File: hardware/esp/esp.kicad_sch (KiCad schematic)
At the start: 37 parts, among them J1 USB_C_Receptacle_USB2.0_16P, J2 Conn_01x02, J3 USB_C_Receptacle_USB2.0_16P, J4 Conn_01x01_Pin, SW1 RESET, SW2 BOOT, U1 AMS1117-3.3, U2 ESP32-S3-WROOM-1, U6 CP2102N-Axx-xQFN20

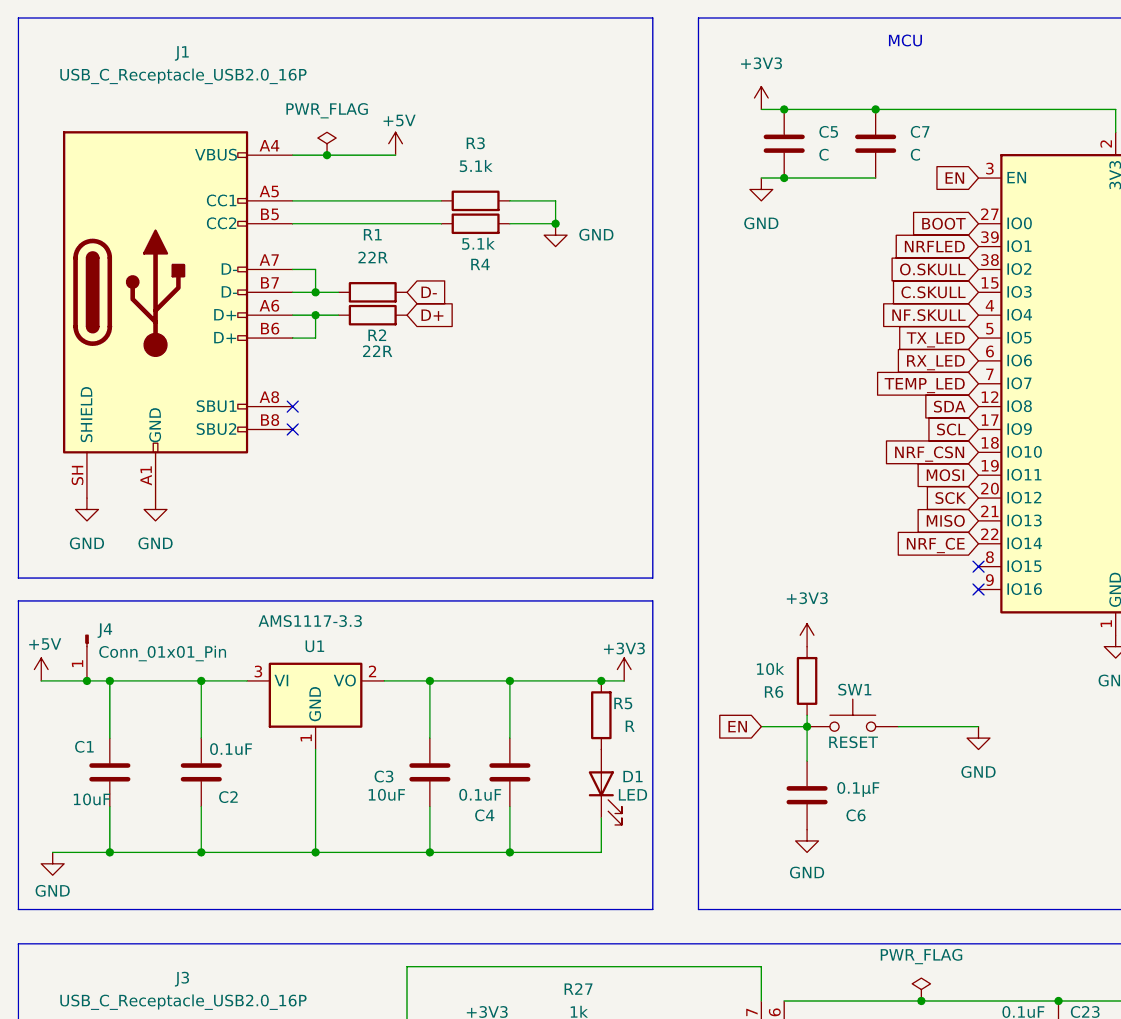
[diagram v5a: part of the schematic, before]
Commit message: Updating schematics and PCB layout
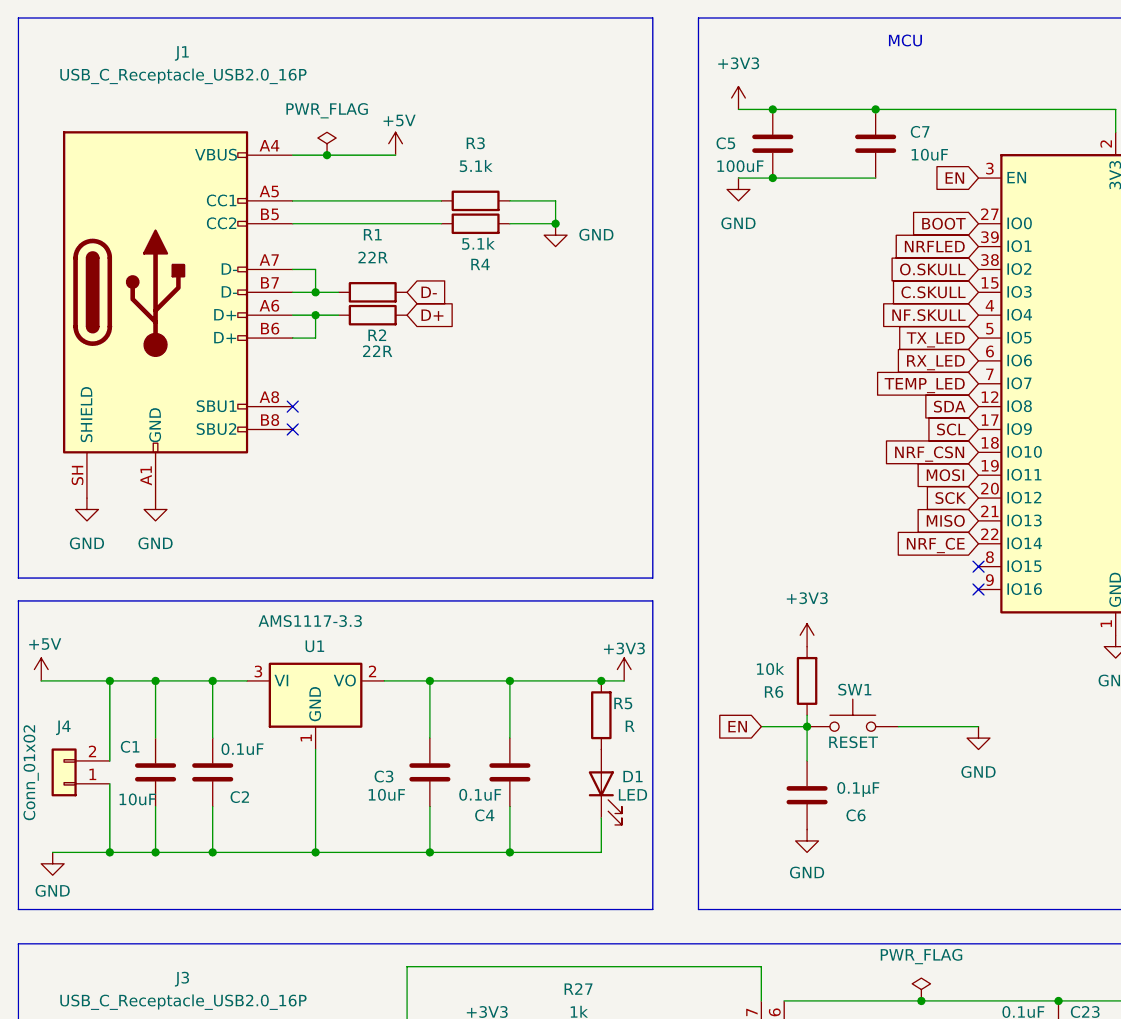
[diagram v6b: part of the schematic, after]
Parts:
- removed J4: Conn_01x01_Pin, Connector_PinHeader_1.00mm:PinHeader_1x01_P1.00mm_Vertical, symbol Connector:Conn_01x01_Pin
- added J4: Conn_01x02, Connector_PinHeader_2.54mm:PinHeader_1x02_P2.54mm_Vertical, symbol Connector_Generic:Conn_01x02
- C5: value C -> 100uF
- C7: value C -> 10uF
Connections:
- net +5V: now also J4.2 (Pin_2)
- net GND: now also J4.1 (Pin_1)
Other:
- moved on the sheet: C1, C2, C5

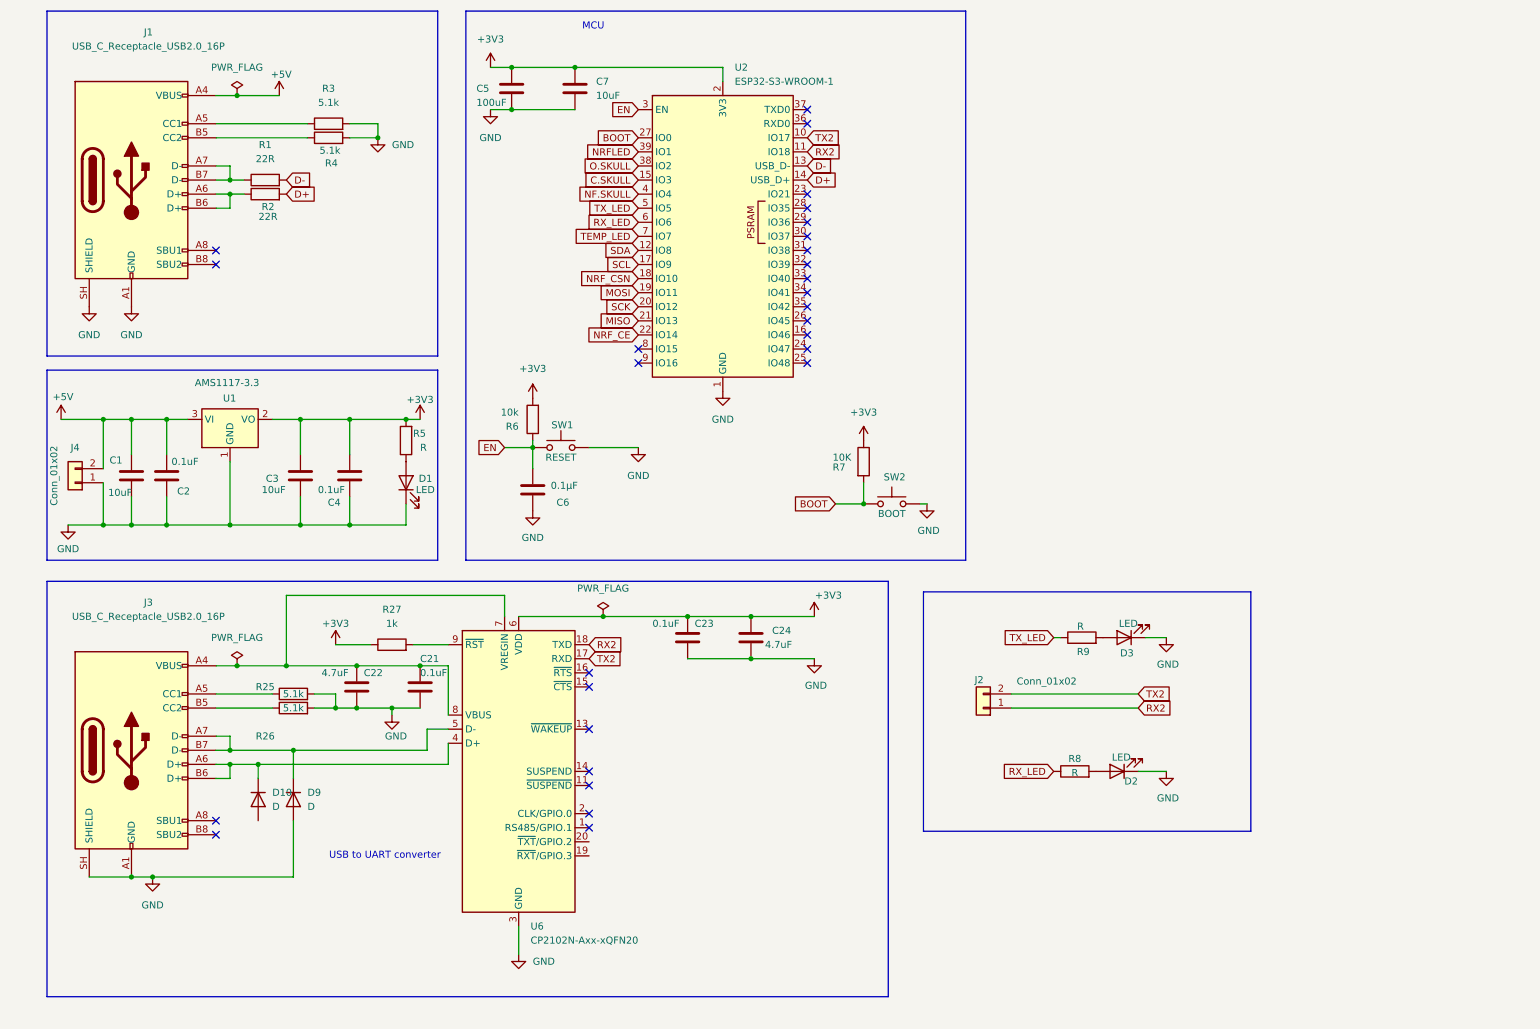
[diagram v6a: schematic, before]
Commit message: Removing UART LEDs
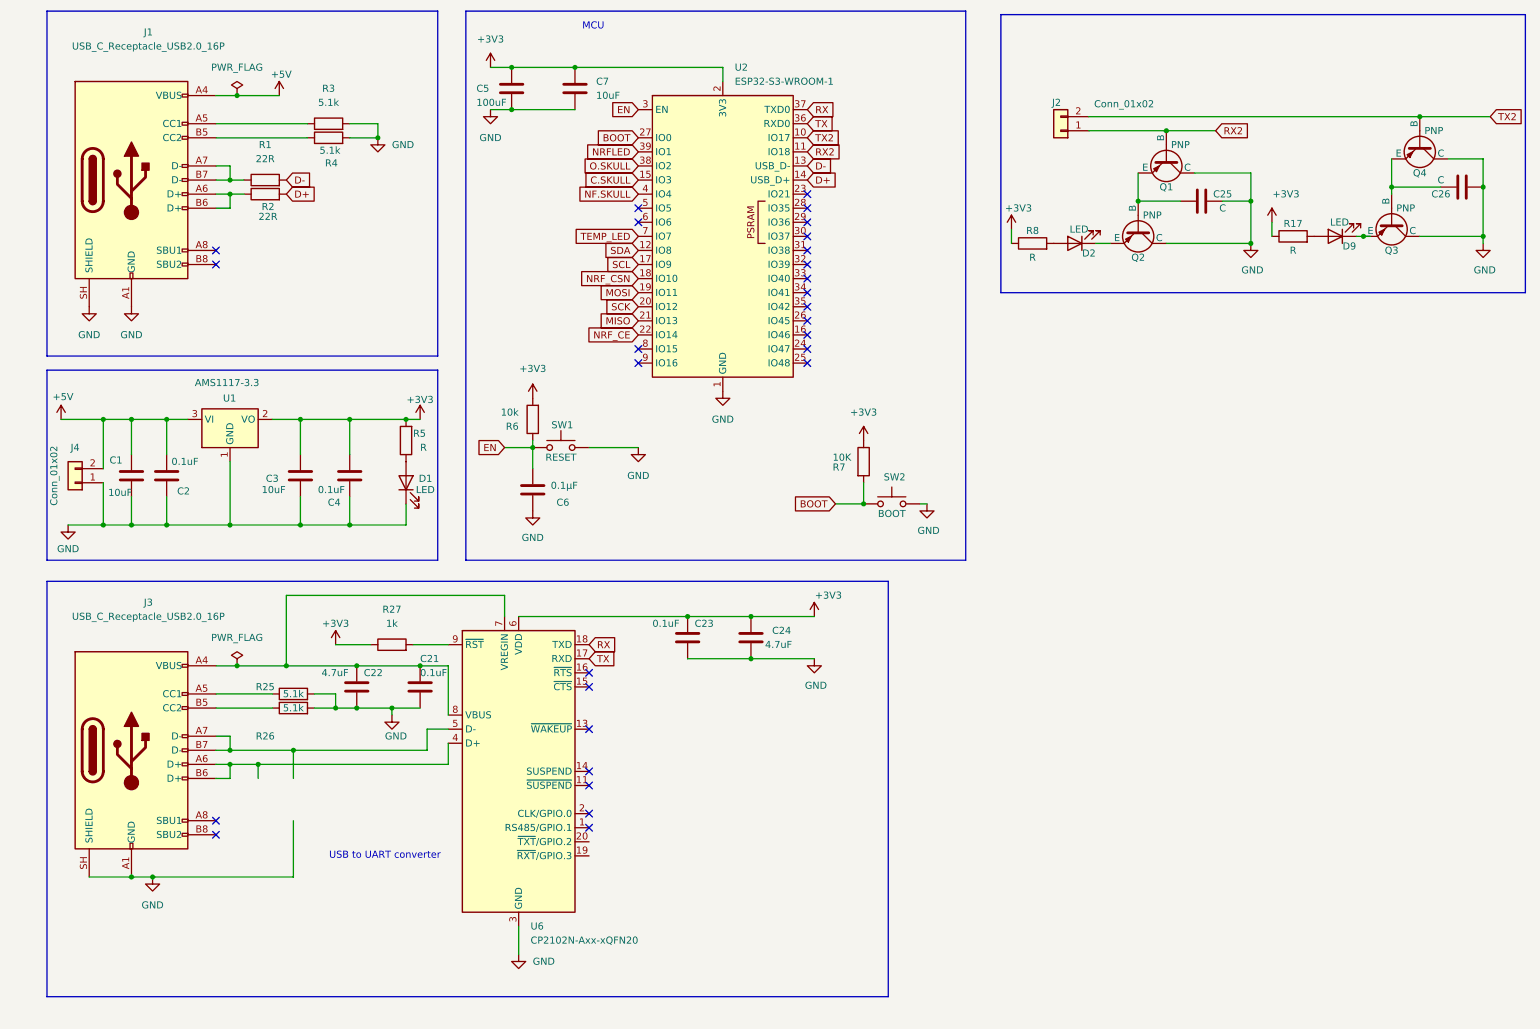
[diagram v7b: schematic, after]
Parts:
- removed D10, D9: D, symbol Device:D
- removed D3: LED, LED_SMD:LED_0603_1608Metric, symbol Device:LED
- removed R9: R, Resistor_SMD:R_0805_2012Metric, symbol Device:R
- added C25, C26: C, symbol Device:C
- added D9: LED, LED_SMD:LED_0603_1608Metric, symbol Device:LED
- added Q1, Q2, Q3, Q4: PNP, symbol Simulation_SPICE:PNP
- added R17: R, Resistor_SMD:R_0805_2012Metric, symbol Device:R
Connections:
- net +3V3: now also R8.1, R17.1
- net GND: now also C25.2, C26.1, Q1.1 (C), Q2.1 (C), Q3.1 (C), Q4.1 (C); no longer D2.1 (K)
- net RX2: now also Q1.2 (B); no longer U6.18 (TXD)
- net TX2: now also Q4.2 (B); no longer U6.17 (RXD)
- net TX: now reaches U2.36 (RXD0)
- net TX: now also U6.17 (RXD)
- net RX: now reaches U2.37 (TXD0)
- net RX: now also U6.18 (TXD)
- net RX_LED: no longer names the net of U2.6 (IO6)
- net RX_LED: no longer R8.1
- net TX_LED: no longer names the net of U2.5 (IO5)
- new net: C25.1, Q1.3 (E), Q2.2 (B)
- new net: C26.2, Q3.2 (B), Q4.3 (E)
- new net: D2.1 (K), Q2.3 (E)
- new net: D9.1 (K), Q3.3 (E)
- new net: D9.2 (A), R17.2
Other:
- moved on the sheet: D2, J2, R8

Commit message: Placing components on PCB and starting routing
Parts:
- C25, C26: footprint (none) -> Capacitor_SMD:C_0805_2012Metric
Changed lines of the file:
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@@
 			)
 		)
-		(property "Footprint" ""
+		(property "Footprint" "Capacitor_SMD:C_0805_2012Metric"
 			(at 267.97 46.6852 0)
 			(hide yes)
@@
 			)
 		)
-		(property "Footprint" ""
+		(property "Footprint" "Capacitor_SMD:C_0805_2012Metric"
 			(at 228.6 47.2948 0)
 			(hide yes)
